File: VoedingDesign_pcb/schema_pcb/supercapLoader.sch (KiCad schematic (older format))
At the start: 20 parts

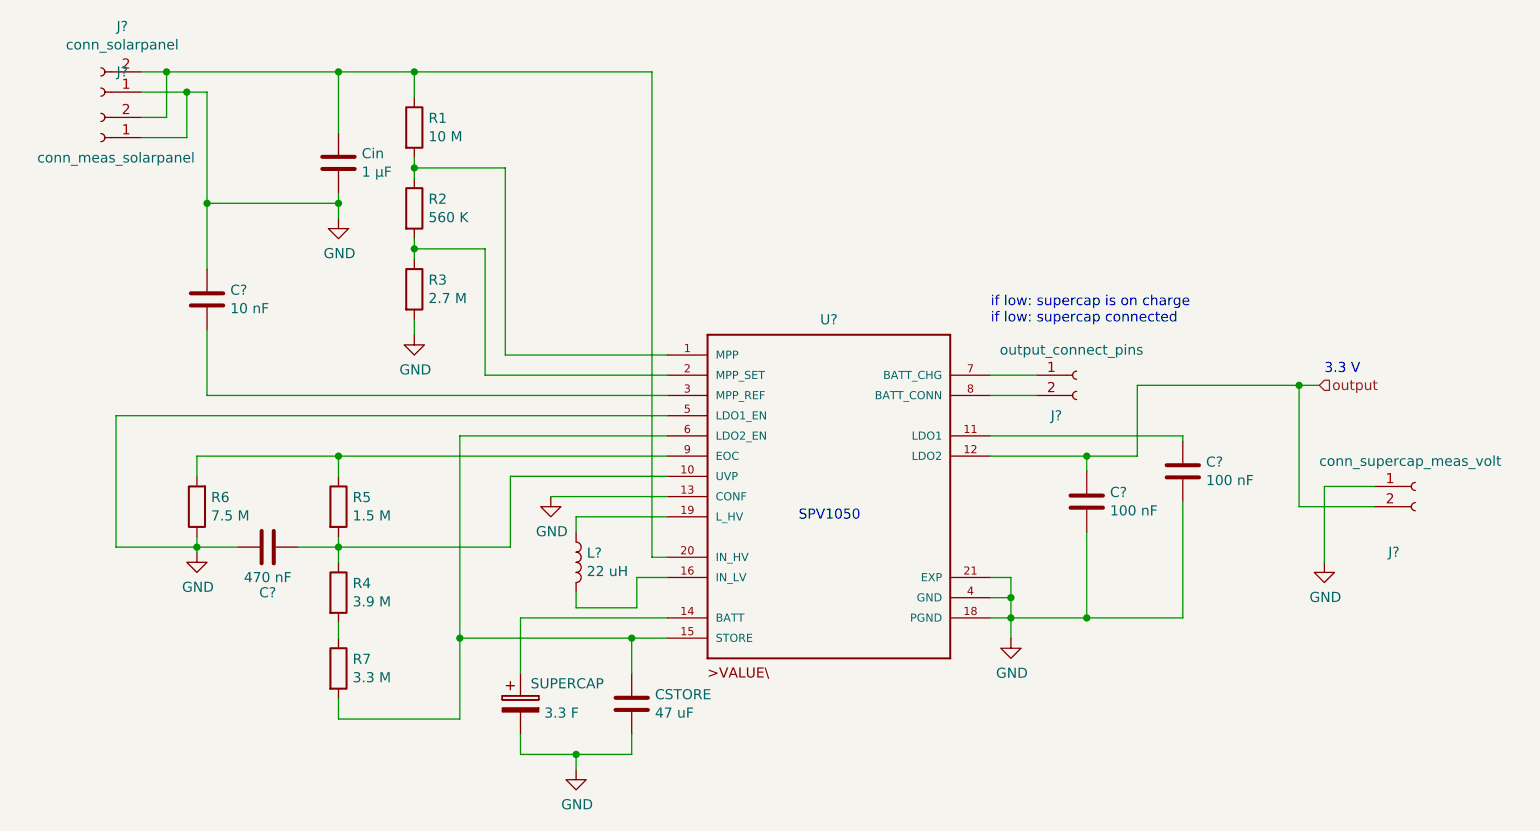
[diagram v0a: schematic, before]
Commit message: schema getekend voeding_ bijna alle footprints volledig
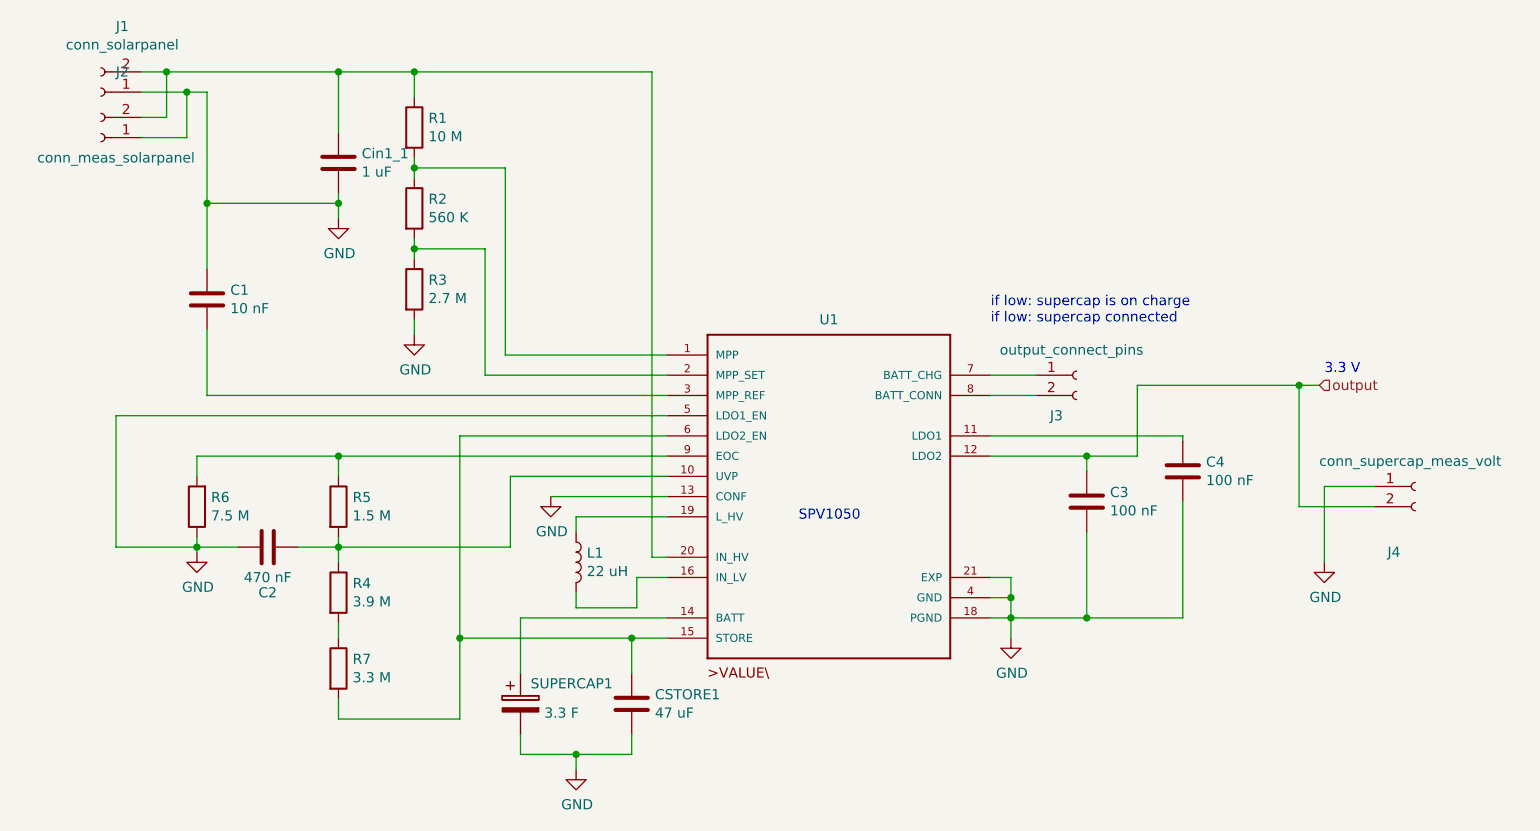
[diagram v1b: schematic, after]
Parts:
- C1, C2, C3, C4: renamed from C?; footprint (none) -> Capacitor_SMD:C_0805_2012Metric_Pad1.15x1.40mm_HandSolder
- CSTORE1: renamed from CSTORE; footprint (none) -> Capacitor_SMD:C_0805_2012Metric_Pad1.15x1.40mm_HandSolder
- Cin1_1: renamed from Cin; value 1 µF -> 1 uF
- J1, J2, J3, J4: renamed from J?; footprint (none) -> Connector_PinHeader_2.54mm:PinHeader_1x02_P2.54mm_Vertical
- R1, R2, R3, R4, R5, R6, R7: footprint (none) -> Resistor_SMD:R_1206_3216Metric_Pad1.42x1.75mm_HandSolder
- SUPERCAP1: renamed from SUPERCAP; footprint (none) -> Capacitor_THT:CP_Radial_D8.0mm_P3.50mm
- U1: renamed from U?; footprint QFN40P300X300X100-21N -> extraFootprints:QFN40P300X300X100-21N
- gave numbers to parts that had none: 1
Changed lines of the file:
@@
 $EndDescr
 $Comp
-L SPV1050TTR:SPV1050TTR U?
+L SPV1050TTR:SPV1050TTR U1
 U 1 1 5E7E12E4
 P 5100 3200
-F 0 "U?" H 5100 4075 50  0000 C CNN
+F 0 "U1" H 5100 4075 50  0000 C CNN
 F 1 "SPV1050TTR" H 5100 3200 50  0001 L BNN
-F 2 "QFN40P300X300X100-21N" H 5100 3200 50  0001 L BNN
+F 2 "extraFootprints:QFN40P300X300X100-21N" H 5100 3200 50  0001 L BNN
 F 3 "ST microelectronics" H 5100 3200 50  0001 L BNN
 	1    5100 3200
@@
 SPV1050
 $Comp
-L power:GND #PWR?
+L power:GND #PWR06
 U 1 1 5E7E1CF5
 P 6000 3900
-F 0 "#PWR?" H 6000 3650 50  0001 C CNN
+F 0 "#PWR06" H 6000 3650 50  0001 C CNN
 F 1 "GND" H 6005 3727 50  0000 C CNN
 F 2 "" H 6000 3900 50  0001 C CNN
@@
 F 0 "R2" H 3120 1821 50  0000 L CNN
 F 1 "560 K" H 3120 1730 50  0000 L CNN
-F 2 "" V 2980 1775 50  0001 C CNN
+F 2 "Resistor_SMD:R_1206_3216Metric_Pad1.42x1.75mm_HandSolder" V 2980 1775 50  0001 C CNN
 F 3 "~" H 3050 1775 50  0001 C CNN
 	1    3050 1775
@@
 F 0 "R3" H 3120 2221 50  0000 L CNN
 F 1 "2.7 M" H 3120 2130 50  0000 L CNN
-F 2 "" V 2980 2175 50  0001 C CNN
+F 2 "Resistor_SMD:R_1206_3216Metric_Pad1.42x1.75mm_HandSolder" V 2980 2175 50  0001 C CNN
 F 3 "~" H 3050 2175 50  0001 C CNN
 	1    3050 2175
@@
 F 0 "R1" H 3120 1421 50  0000 L CNN
 F 1 "10 M" H 3120 1330 50  0000 L CNN
-F 2 "" V 2980 1375 50  0001 C CNN
+F 2 "Resistor_SMD:R_1206_3216Metric_Pad1.42x1.75mm_HandSolder" V 2980 1375 50  0001 C CNN
 F 3 "~" H 3050 1375 50  0001 C CNN
 	1    3050 1375
@@
 $EndComp
 $Comp
-L Device:C Cin
+L Device:C Cin1_1
 U 1 1 5E7E428F
 P 2675 1550
-F 0 "Cin" H 2790 1596 50  0000 L CNN
-F 1 "1 µF" H 2790 1505 50  0000 L CNN
+F 0 "Cin1_1" H 2790 1596 50  0000 L CNN
+F 1 "1 uF" H 2790 1505 50  0000 L CNN
 F 2 "" H 2713 1400 50  0001 C CNN
 F 3 "~" H 2675 1550 50  0001 C CNN
@@
 $EndComp
 $Comp
-L Device:C C?
+L Device:C C1
 U 1 1 5E7E4354
 P 2025 2225
-F 0 "C?" H 2140 2271 50  0000 L CNN
+F 0 "C1" H 2140 2271 50  0000 L CNN
 F 1 "10 nF" H 2140 2180 50  0000 L CNN
-F 2 "" H 2063 2075 50  0001 C CNN
+F 2 "Capacitor_SMD:C_0805_2012Metric_Pad1.15x1.40mm_HandSolder" H 2063 2075 50  0001 C CNN
 F 3 "~" H 2025 2225 50  0001 C CNN
 	1    2025 2225
@@
 	3050 1575 3050 1625
 $Comp
-L power:GND #PWR?
+L power:GND #PWR02
 U 1 1 5E7E538D
 P 2675 1825
-F 0 "#PWR?" H 2675 1575 50  0001 C CNN
+F 0 "#PWR02" H 2675 1575 50  0001 C CNN
 F 1 "GND" H 2680 1652 50  0000 C CNN
 F 2 "" H 2675 1825 50  0001 C CNN
@@
 	2675 1750 2675 1825
 $Comp
-L Connector:Conn_01x02_Female J?
+L Connector:Conn_01x02_Female J1
 U 1 1 5E7E5DEE
 P 1500 1200
-F 0 "J?" H 1394 875 50  0000 C CNN
+F 0 "J1" H 1394 875 50  0000 C CNN
 F 1 "conn_solarpanel" H 1394 966 50  0000 C CNN
-F 2 "" H 1500 1200 50  0001 C CNN
+F 2 "Connector_PinHeader_2.54mm:PinHeader_1x02_P2.54mm_Vertical" H 1500 1200 50  0001 C CNN
 F 3 "~" H 1500 1200 50  0001 C CNN
 	1    1500 1200
@@
 	2675 1100 3050 1100
 $Comp
-L Device:L L?
+L Device:L L1
 U 1 1 5E7E7325
 P 3850 3525
-F 0 "L?" H 3903 3571 50  0000 L CNN
+F 0 "L1" H 3903 3571 50  0000 L CNN
 F 1 "22 uH" H 3903 3480 50  0000 L CNN
 F 2 "" H 3850 3525 50  0001 C CNN
@@
 	4150 3600 4300 3600
 $Comp
-L Device:C C?
+L Device:C C4
 U 1 1 5E7E801B
 P 6850 3075
-F 0 "C?" H 6965 3121 50  0000 L CNN
+F 0 "C4" H 6965 3121 50  0000 L CNN
 F 1 "100 nF" H 6965 3030 50  0000 L CNN
-F 2 "" H 6888 2925 50  0001 C CNN
+F 2 "Capacitor_SMD:C_0805_2012Metric_Pad1.15x1.40mm_HandSolder" H 6888 2925 50  0001 C CNN
 F 3 "~" H 6850 3075 50  0001 C CNN
 	1    6850 3075
@@
 $EndComp
 $Comp
-L Device:C C?
+L Device:C C3
 U 1 1 5E7E80E8
 P 6375 3225
-F 0 "C?" H 6490 3271 50  0000 L CNN
+F 0 "C3" H 6490 3271 50  0000 L CNN
 F 1 "100 nF" H 6490 3180 50  0000 L CNN
-F 2 "" H 6413 3075 50  0001 C CNN
+F 2 "Capacitor_SMD:C_0805_2012Metric_Pad1.15x1.40mm_HandSolder" H 6413 3075 50  0001 C CNN
 F 3 "~" H 6375 3225 50  0001 C CNN
 	1    6375 3225
@@
 Connection ~ 6375 3000
 $Comp
-L Device:C CSTORE
+L Device:C CSTORE1
 U 1 1 5E7EB0D9
 P 4125 4225
-F 0 "CSTORE" H 4240 4271 50  0000 L CNN
+F 0 "CSTORE1" H 4240 4271 50  0000 L CNN
 F 1 "47 uF" H 4240 4180 50  0000 L CNN
-F 2 "" H 4163 4075 50  0001 C CNN
+F 2 "Capacitor_SMD:C_0805_2012Metric_Pad1.15x1.40mm_HandSolder" H 4163 4075 50  0001 C CNN
 F 3 "~" H 4125 4225 50  0001 C CNN
 	1    4125 4225
@@
 	3575 3800 4300 3800
 $Comp
-L power:GND #PWR?
+L power:GND #PWR05
 U 1 1 5E7ED156
 P 3850 4550
-F 0 "#PWR?" H 3850 4300 50  0001 C CNN
+F 0 "#PWR05" H 3850 4300 50  0001 C CNN
 F 1 "GND" H 3855 4377 50  0000 C CNN
 F 2 "" H 3850 4550 50  0001 C CNN
@@
 Connection ~ 3850 4475
 $Comp
-L power:GND #PWR?
+L power:GND #PWR03
 U 1 1 5E7F1643
 P 3050 2400
-F 0 "#PWR?" H 3050 2150 50  0001 C CNN
+F 0 "#PWR03" H 3050 2150 50  0001 C CNN
 F 1 "GND" H 3055 2227 50  0000 C CNN
 F 2 "" H 3050 2400 50  0001 C CNN
@@
 $EndComp
 $Comp
-L power:GND #PWR?
+L power:GND #PWR04
 U 1 1 5E7F1666
 P 3725 3200
-F 0 "#PWR?" H 3725 2950 50  0001 C CNN
+F 0 "#PWR04" H 3725 2950 50  0001 C CNN
 F 1 "GND" H 3730 3027 50  0000 C CNN
 F 2 "" H 3725 3200 50  0001 C CNN
@@
 F 0 "R4" H 2745 3721 50  0000 L CNN
 F 1 "3.9 M" H 2745 3630 50  0000 L CNN
-F 2 "" V 2605 3675 50  0001 C CNN
+F 2 "Resistor_SMD:R_1206_3216Metric_Pad1.42x1.75mm_HandSolder" V 2605 3675 50  0001 C CNN
 F 3 "~" H 2675 3675 50  0001 C CNN
 	1    2675 3675
@@
 F 0 "R5" H 2745 3296 50  0000 L CNN
 F 1 "1.5 M" H 2745 3205 50  0000 L CNN
-F 2 "" V 2605 3250 50  0001 C CNN
+F 2 "Resistor_SMD:R_1206_3216Metric_Pad1.42x1.75mm_HandSolder" V 2605 3250 50  0001 C CNN
 F 3 "~" H 2675 3250 50  0001 C CNN
 	1    2675 3250
@@
 F 0 "R6" H 1905 3204 50  0000 R CNN
 F 1 "7.5 M" H 1905 3295 50  0000 R CNN
-F 2 "" V 1905 3250 50  0001 C CNN
+F 2 "Resistor_SMD:R_1206_3216Metric_Pad1.42x1.75mm_HandSolder" V 1905 3250 50  0001 C CNN
 F 3 "~" H 1975 3250 50  0001 C CNN
 	1    1975 3250
@@
 	1975 3000 1975 3100
 $Comp
-L power:GND #PWR?
+L power:GND #PWR01
 U 1 1 5E7FB2BD
 P 1975 3475
-F 0 "#PWR?" H 1975 3225 50  0001 C CNN
+F 0 "#PWR01" H 1975 3225 50  0001 C CNN
 F 1 "GND" H 1980 3302 50  0000 C CNN
 F 2 "" H 1975 3475 50  0001 C CNN
@@
 F 0 "R7" H 2745 4096 50  0000 L CNN
 F 1 "3.3 M" H 2745 4005 50  0000 L CNN
-F 2 "" V 2605 4050 50  0001 C CNN
+F 2 "Resistor_SMD:R_1206_3216Metric_Pad1.42x1.75mm_HandSolder" V 2605 4050 50  0001 C CNN
 F 3 "~" H 2675 4050 50  0001 C CNN
 	1    2675 4050
@@
 Connection ~ 2675 3000
 $Comp
-L Device:C C?
+L Device:C C2
 U 1 1 5E81487A
 P 2325 3450
-F 0 "C?" V 2550 3450 50  0000 C CNN
+F 0 "C2" V 2550 3450 50  0000 C CNN
 F 1 "470 nF" V 2475 3450 50  0000 C CNN
-F 2 "" H 2363 3300 50  0001 C CNN
+F 2 "Capacitor_SMD:C_0805_2012Metric_Pad1.15x1.40mm_HandSolder" H 2363 3300 50  0001 C CNN
 F 3 "~" H 2325 3450 50  0001 C CNN
 	1    2325 3450
@@
 3.3 V
 $Comp
-L Connector:Conn_01x02_Female J?
+L Connector:Conn_01x02_Female J4
 U 1 1 5E820395
 P 8000 3150
-F 0 "J?" H 7894 2825 50  0000 C CNN
+F 0 "J4" H 7894 2825 50  0000 C CNN
 F 1 "conn_supercap_meas_volt" H 7975 3275 50  0000 C CNN
-F 2 "" H 8000 3150 50  0001 C CNN
+F 2 "Connector_PinHeader_2.54mm:PinHeader_1x02_P2.54mm_Vertical" H 8000 3150 50  0001 C CNN
 F 3 "~" H 8000 3150 50  0001 C CNN
 	1    8000 3150
@@
 $EndComp
 $Comp
-L Connector:Conn_01x02_Female J?
+L Connector:Conn_01x02_Female J2
 U 1 1 5E82056B
 P 1500 1425
-F 0 "J?" H 1394 1100 50  0000 C CNN
+F 0 "J2" H 1394 1100 50  0000 C CNN
 F 1 "conn_meas_solarpanel" H 1425 1525 50  0000 C CNN
-F 2 "" H 1500 1425 50  0001 C CNN
+F 2 "Connector_PinHeader_2.54mm:PinHeader_1x02_P2.54mm_Vertical" H 1500 1425 50  0001 C CNN
 F 3 "~" H 1500 1425 50  0001 C CNN
 	1    1500 1425
@@
 	7425 2650 7425 3250
 $Comp
-L power:GND #PWR?
+L power:GND #PWR07
 U 1 1 5E829443
 P 7550 3525
-F 0 "#PWR?" H 7550 3275 50  0001 C CNN
+F 0 "#PWR07" H 7550 3275 50  0001 C CNN
 F 1 "GND" H 7555 3352 50  0000 C CNN
 F 2 "" H 7550 3525 50  0001 C CNN
@@
 	7550 3150 7800 3150
 $Comp
-L Connector:Conn_01x02_Female J?
+L Connector:Conn_01x02_Female J3
 U 1 1 5E82BD4A
 P 6325 2600
-F 0 "J?" H 6225 2400 50  0000 C CNN
+F 0 "J3" H 6225 2400 50  0000 C CNN
 F 1 "output_connect_pins" H 6300 2725 50  0000 C CNN
-F 2 "" H 6325 2600 50  0001 C CNN
+F 2 "Connector_PinHeader_2.54mm:PinHeader_1x02_P2.54mm_Vertical" H 6325 2600 50  0001 C CNN
 F 3 "~" H 6325 2600 50  0001 C CNN
 	1    6325 2600
@@
 Connection ~ 6000 3700
 $Comp
-L Device:CP SUPERCAP
+L Device:CP SUPERCAP1
 U 1 1 5E833869
 P 3575 4225
-F 0 "SUPERCAP" H 3625 4325 50  0000 L CNN
+F 0 "SUPERCAP1" H 3625 4325 50  0000 L CNN
 F 1 "3.3 F" H 3693 4180 50  0000 L CNN
-F 2 "" H 3613 4075 50  0001 C CNN
+F 2 "Capacitor_THT:CP_Radial_D8.0mm_P3.50mm" H 3613 4075 50  0001 C CNN
 F 3 "~" H 3575 4225 50  0001 C CNN
 	1    3575 4225

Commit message: afgewerkte Energy Harvesting PCB
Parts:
- CSTORE1: footprint Capacitor_SMD:C_0805_2012Metric_Pad1.15x1.40mm_HandSolder -> Capacitor_SMD:CP_Elec_6.3x5.3
- Cin1_1: footprint (none) -> Capacitor_SMD:C_0603_1608Metric_Pad1.05x0.95mm_HandSolder
- L1: footprint (none) -> Inductor_SMD:L_Coilcraft_XxL4040
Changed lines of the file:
@@
 F 0 "Cin1_1" H 2790 1596 50  0000 L CNN
 F 1 "1 uF" H 2790 1505 50  0000 L CNN
-F 2 "" H 2713 1400 50  0001 C CNN
+F 2 "Capacitor_SMD:C_0603_1608Metric_Pad1.05x0.95mm_HandSolder" H 2713 1400 50  0001 C CNN
 F 3 "~" H 2675 1550 50  0001 C CNN
 	1    2675 1550
@@
 F 0 "L1" H 3903 3571 50  0000 L CNN
 F 1 "22 uH" H 3903 3480 50  0000 L CNN
-F 2 "" H 3850 3525 50  0001 C CNN
+F 2 "Inductor_SMD:L_Coilcraft_XxL4040" H 3850 3525 50  0001 C CNN
 F 3 "~" H 3850 3525 50  0001 C CNN
 	1    3850 3525
@@
 F 0 "CSTORE1" H 4240 4271 50  0000 L CNN
 F 1 "47 uF" H 4240 4180 50  0000 L CNN
-F 2 "Capacitor_SMD:C_0805_2012Metric_Pad1.15x1.40mm_HandSolder" H 4163 4075 50  0001 C CNN
+F 2 "Capacitor_SMD:CP_Elec_6.3x5.3" H 4163 4075 50  0001 C CNN
 F 3 "~" H 4125 4225 50  0001 C CNN
 	1    4125 4225
